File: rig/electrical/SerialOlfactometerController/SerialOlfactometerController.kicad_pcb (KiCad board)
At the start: 2 copper layers, 104.1 x 104.1 mm, 34 parts, among them J1 Screw_Terminal_01x02, J10 Screw_Terminal_01x02, J11 Screw_Terminal_01x02, J12 Screw_Terminal_01x02, J13 Screw_Terminal_01x02, J14 Screw_Terminal_01x02, J15 Screw_Terminal_01x02, J16 Screw_Terminal_01x02, J17 Conn_01x05_Socket, J18 TST-105-01-X-D, J19 TST-105-01-X-D, J2 Screw_Terminal_01x02, J3 Screw_Terminal_01x02, J4 Screw_Terminal_01x02, J5 Screw_Terminal_01x02, J6 Screw_Terminal_01x02, J7 Screw_Terminal_01x02, J8 Screw_Terminal_01x02, J9 Screw_Terminal_01x02, U1 TPIC6595, U2 TPIC6595

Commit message: Serial Olfactometer improved design
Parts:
- added TP1: TestPoint, TestPoint:TestPoint_Pad_2.0x2.0mm, B.Cu at (148.3, 81.6)
- added TP2: TestPoint, TestPoint:TestPoint_Pad_2.0x2.0mm, B.Cu at (169.0, 73.5)
- added TP3: TestPoint, TestPoint:TestPoint_Pad_2.0x2.0mm, B.Cu at (140.5, 82.0)
- added TP4: TestPoint, TestPoint:TestPoint_Pad_2.0x2.0mm, B.Cu at (131.3, 66.3)
- added TP5: TestPoint, TestPoint:TestPoint_Pad_2.0x2.0mm, B.Cu at (135.4, 122.2)
- added TP6: TestPoint, TestPoint:TestPoint_Pad_2.0x2.0mm, B.Cu at (122.2, 110.4)
- R3, R4, R5, R6, R7: value R -> 33Ω
- turned J10 to -146 degrees
- turned J14 to -56 degrees
- turned J15 to -34 degrees
- turned J2 to 34 degrees
- turned J3 to 56 degrees
- turned J7 to 146 degrees
- turned J11 to -124 degrees
- turned J6 to 124 degrees
- turned J12 to -101 degrees
- turned J13 to -79 degrees
- turned J8 to 169 degrees
- turned J9 to -169 degrees
- turned J1 to 11 degrees
- turned J16 to -11 degrees
- turned J4 to 79 degrees
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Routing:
- net Net-(J3-Pin_1): track 44.3 -> 56.6 mm
- net +24V: track 368.3 -> 376.6 mm
- net Net-(J7-Pin_1): track 21.9 -> 27.8 mm
- net Net-(U2-SER_OUT): track 62.5 -> 68.2 mm
- net Net-(J16-Pin_1): track 59.3 -> 61.9 mm
- net +5V: track 81.5 -> 84.0 mm
- net Net-(U1-SRCK): track 161.8 -> 164.1 mm
- net Net-(J18-Pad06): track 21.3 -> 23.0 mm
- net Net-(U1-SER_IN): track 74.8 -> 73.6 mm
- net Net-(J18-Pad01): track 20.5 -> 21.7 mm
- net Net-(J18-Pad04): track 21.3 -> 22.1 mm
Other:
- board text added: "+24V"
- board text added: "0.1μF"
- board text added: "10kΩ"
- board text added: "10μF"
- board text added: "33Ω"
- board text added: "CABLE -> SERIAL IN"
- board text added: "CLOCK IN"
- board text added: "CLOCK OUT"
- board text added: "GND"
- board text added: "LATCH"
- board text added: "SERIAL OUT -> CABLE"
- board text added: "SERIAL OUT -> IN"
- board text added: "USE A SHORT HEADER TO CONNECT APPROPRIATE INPUT TO OUTPUT"
- board text removed: "USE A SHORT HEADER CABLE TO CONNECT THE APPROPRIATE INPUT TO OUTPUT"

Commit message: Tweaking of v1 boards
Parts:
- removed H1, H2: MountingHole, MountingHole:MountingHole_3.2mm_M3_DIN965_Pad
- added H3: MountingHole_Pad, MountingHole:MountingHole_3.2mm_M3_Pad, F.Cu at (164.6, 90.9)
- added H4: MountingHole_Pad, MountingHole:MountingHole_3.2mm_M3_Pad, F.Cu at (113.8, 90.9)
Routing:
- net +5V: track 84.0 -> 94.3 mm

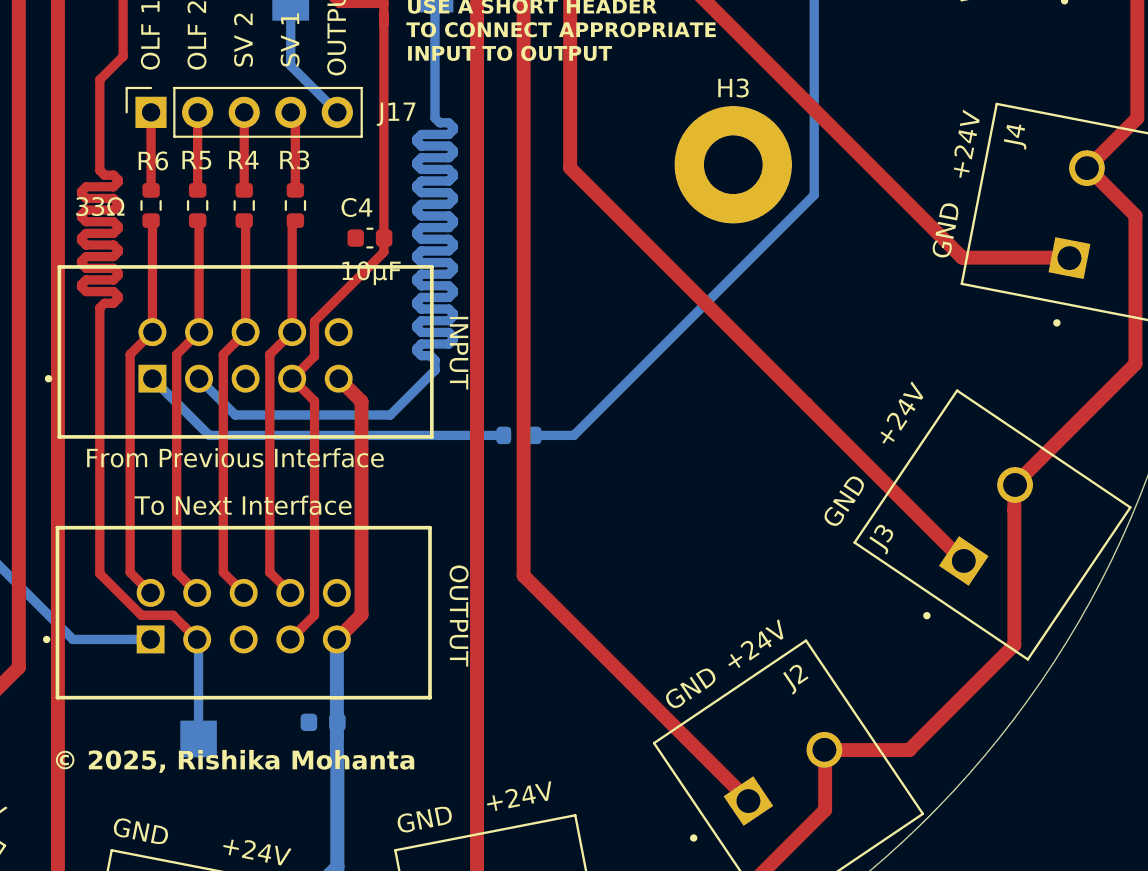
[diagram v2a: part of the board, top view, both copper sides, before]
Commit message: Termination Resistors/GND Vias
Added termination resistors to avoid reflections on signal lines. Added vias to GND plane stubs to avoid antennae effects.
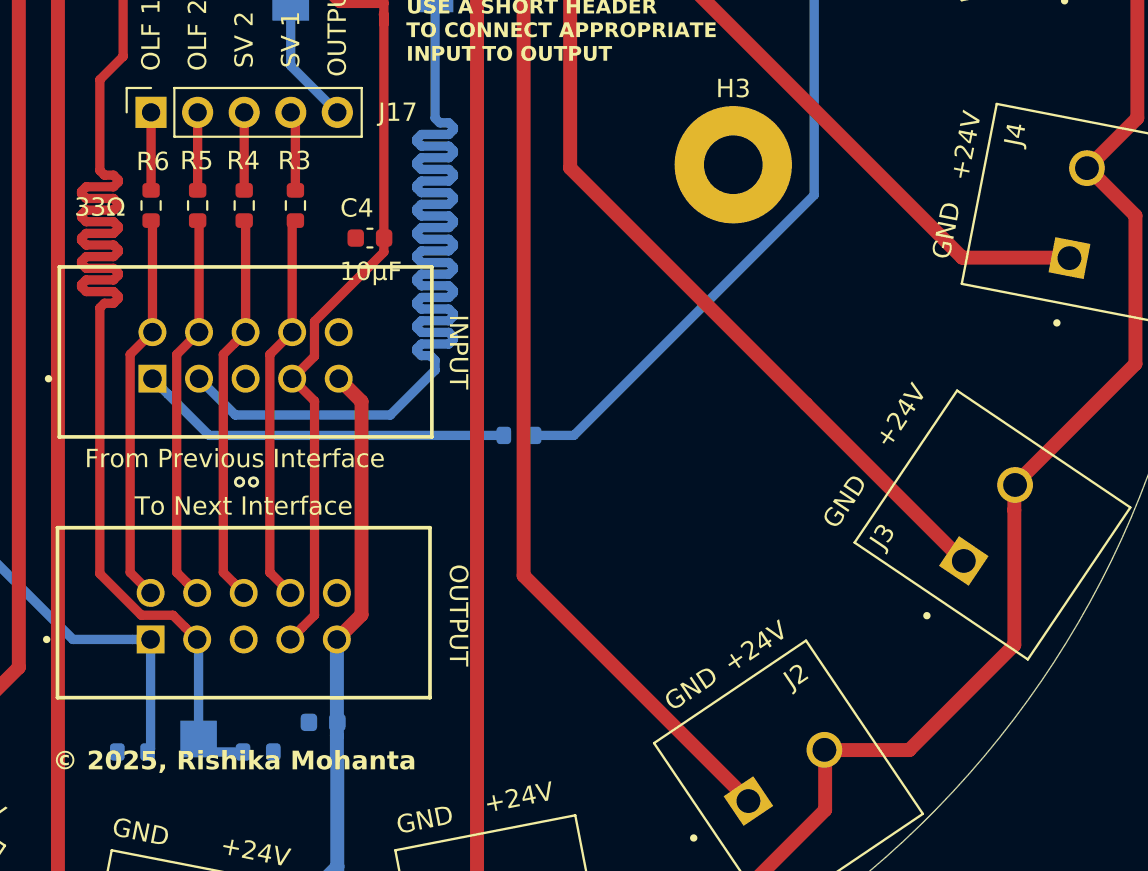
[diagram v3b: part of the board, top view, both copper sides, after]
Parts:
- added R8: Term_Imp, Resistor_SMD:R_0603_1608Metric, B.Cu at (131.8, 122.9)
- added R9: Term_Imp, Resistor_SMD:R_0603_1608Metric, B.Cu at (138.7, 122.9)
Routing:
- net Net-(U1-SRCK): track 164.1 -> 170.3 mm
- net Net-(U2-SER_OUT): track 68.2 -> 71.0 mm
- net GND: vias 0 -> 2
